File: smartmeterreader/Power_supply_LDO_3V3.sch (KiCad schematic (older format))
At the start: 5 parts

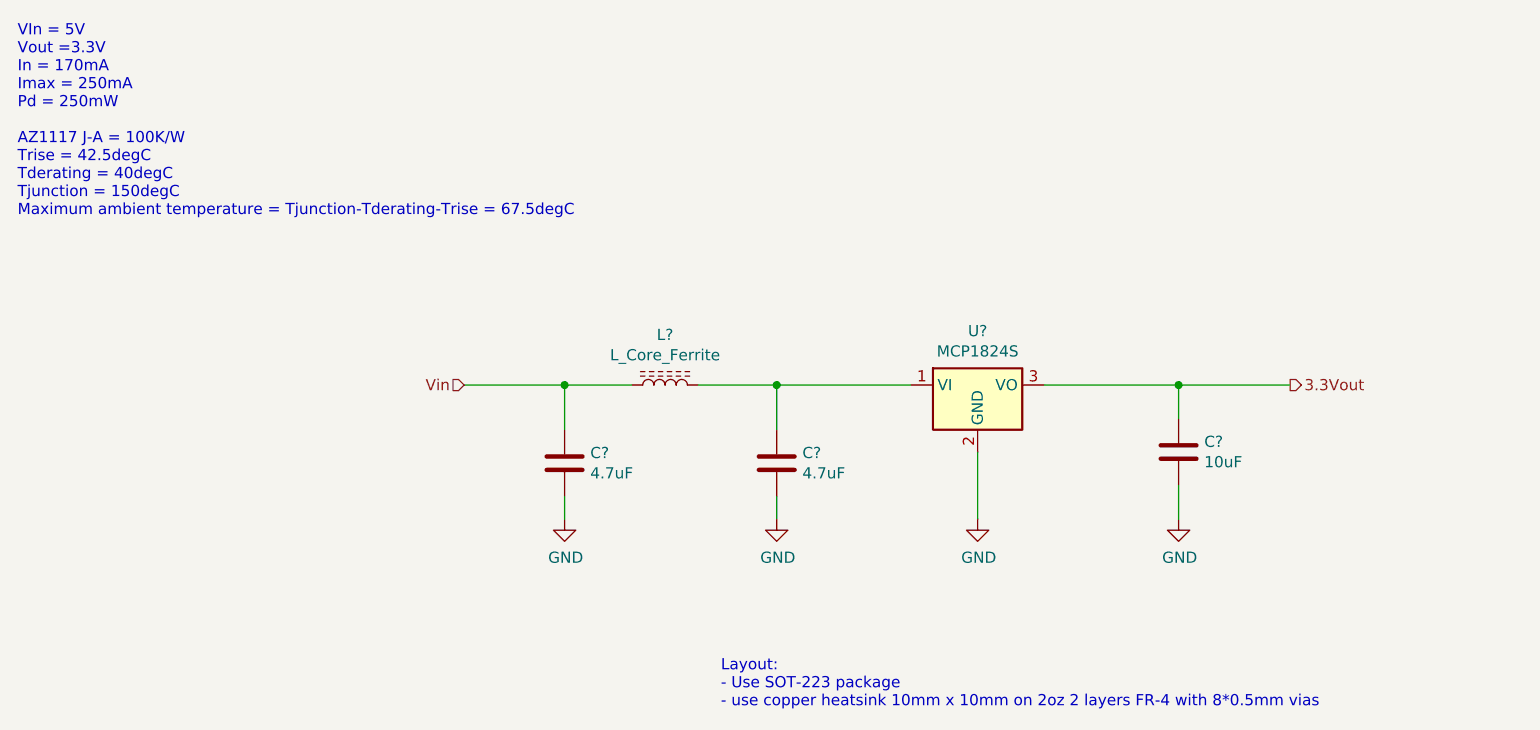
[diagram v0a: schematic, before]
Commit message: Initial version of the smart meter. -Needs compoonent review, - Needs schematics review - No layout
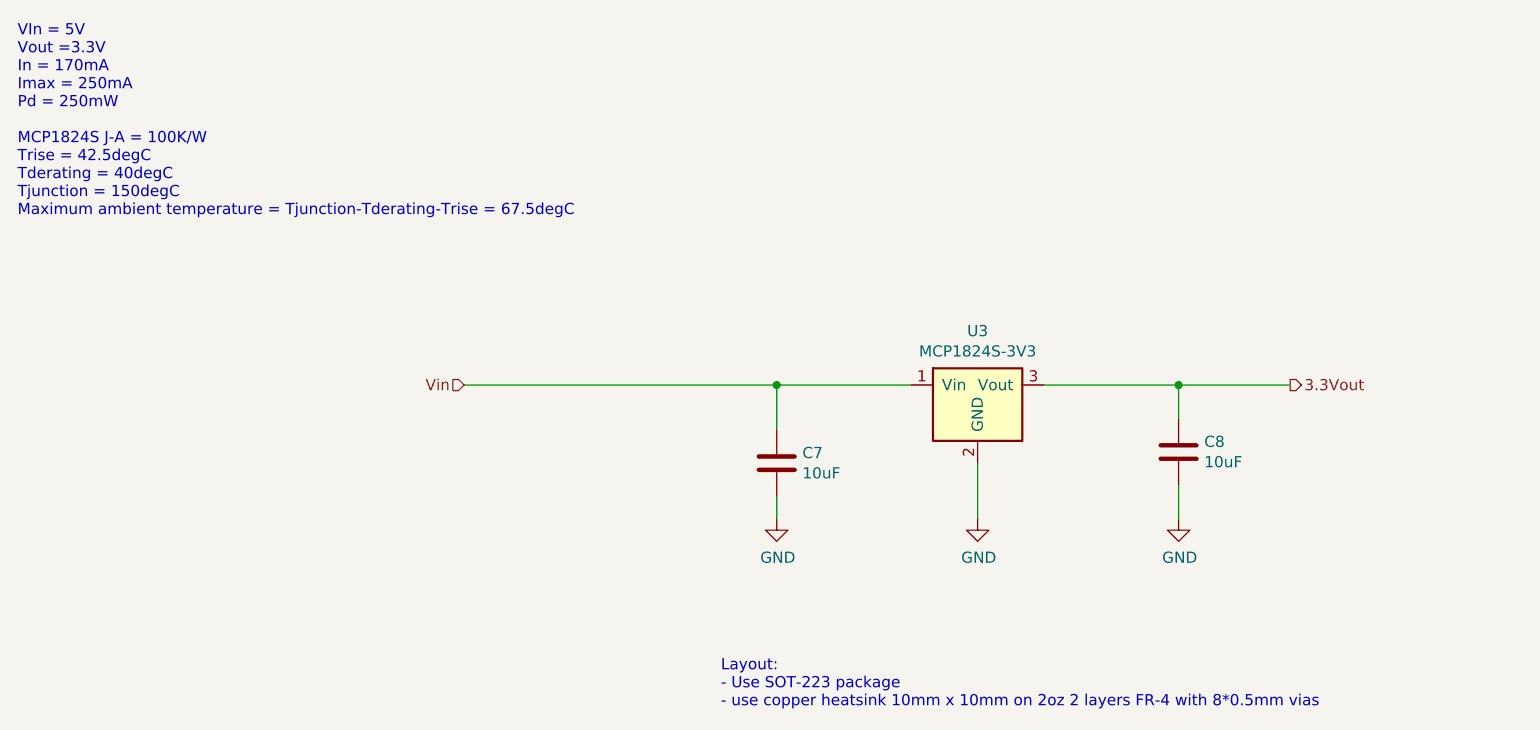
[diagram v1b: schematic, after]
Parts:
- removed C? (x2): 4.7uF, Capacitor_SMD:C_0805_2012Metric, symbol Capacitor_Ceramic_SMD_0603:4.7uF
- removed C?: 10uF, Capacitor_SMD:C_0805_2012Metric, symbol Capacitor_Ceramic_SMD_0603:10uF
- removed L?: L_Core_Ferrite, symbol Device:L_Core_Ferrite
- removed U?: MCP1824S, symbol Regulator_Linear:MCP1825S
- added C7, C8: 10uF, Capacitor_SMD:C_0805_2012Metric, symbol Capacitor_Ceramic_SMD_0603:10uF
- added U3: MCP1824S-3V3, Package_TO_SOT_SMD:SOT-223-3_TabPin2, symbol IC_Power_Regulator:MCP1824S-3V3
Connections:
- net 3.3Vout: now also C8.1, U3.3 (Vout)
- net GND: now also C7.2, C8.2, U3.2 (GND)
- net Vin: now also C7.1, U3.1 (Vin)
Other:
- note added: "VIn = 5V\nVout =3.3V\nIn = 170mA\nImax = 250mA\nPd = 250mW\n\nMCP1824S J-A = 100K/W\nTrise = 42.5degC\nTderating = 40degC\nTjunction = 150degC\nMaximum ambient temperature = Tjunction-Tderating-Trise = 67.5degC"
- note removed: "VIn = 5V\nVout =3.3V\nIn = 170mA\nImax = 250mA\nPd = 250mW\n\nAZ1117 J-A = 100K/W\nTrise = 42.5degC\nTderating = 40degC\nTjunction = 150degC\nMaximum ambient temperature = Tjunction-Tderating-Trise = 67.5degC"
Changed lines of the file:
@@
 $Descr A4 11693 8268
 encoding utf-8
-Sheet 3 3
-Title ""
+Sheet 3 5
+Title "Power supply LDO 300mA 200mV droput"
 Date ""
 Rev ""
-Comp ""
-Comment1 ""
+Comp "ODiaz"
+Comment1 "Orlando Diaz"
 Comment2 ""
 Comment3 ""
@@
 $EndDescr
 Text Notes 1550 2650 0    50   ~ 0
-VIn = 5V\nVout =3.3V\nIn = 170mA\nImax = 250mA\nPd = 250mW\n\nAZ1117 J-A = 100K/W\nTrise = 42.5degC\nTderating = 40degC\nTjunction = 150degC\nMaximum ambient temperature = Tjunction-Tderating-Trise = 67.5degC
+VIn = 5V\nVout =3.3V\nIn = 170mA\nImax = 250mA\nPd = 250mW\n\nMCP1824S J-A = 100K/W\nTrise = 42.5degC\nTderating = 40degC\nTjunction = 150degC\nMaximum ambient temperature = Tjunction-Tderating-Trise = 67.5degC
 Text Notes 4700 4850 0    50   ~ 0
 Layout:\n- Use SOT-223 package\n- use copper heatsink 10mm x 10mm on 2oz 2 layers FR-4 with 8*0.5mm vias
+Wire Wire Line
+	4950 3600 4950 3400
+Wire Wire Line
+	6750 3400 6750 3550
 $Comp
-L Regulator_Linear:MCP1825S U?
-U 1 1 61B7A6BC
+L power:GND #PWR019
+U 1 1 61B7D793
+P 5850 4000
+F 0 "#PWR019" H 5850 3750 50  0001 C CNN
+F 1 "GND" H 5855 3827 50  0000 C CNN
+F 2 "" H 5850 4000 50  0001 C CNN
+F 3 "" H 5850 4000 50  0001 C CNN
+	1    5850 4000
+	1    0    0    -1
+$EndComp
+$Comp
+L power:GND #PWR018
+U 1 1 61B7DB62
+P 4950 4000
+F 0 "#PWR018" H 4950 3750 50  0001 C CNN
+F 1 "GND" H 4955 3827 50  0000 C CNN
+F 2 "" H 4950 4000 50  0001 C CNN
+F 3 "" H 4950 4000 50  0001 C CNN
+	1    4950 4000
+	1    0    0    -1
+$EndComp
+$Comp
+L power:GND #PWR020
+U 1 1 61B7DED9
+P 6750 4000
+F 0 "#PWR020" H 6750 3750 50  0001 C CNN
+F 1 "GND" H 6755 3827 50  0000 C CNN
+F 2 "" H 6750 4000 50  0001 C CNN
+F 3 "" H 6750 4000 50  0001 C CNN
+	1    6750 4000
+	1    0    0    -1
+$EndComp
+Wire Wire Line
+	6750 4000 6750 3850
+Wire Wire Line
+	5850 4000 5850 3750
+Wire Wire Line
+	4950 4000 4950 3900
+Wire Wire Line
+	6150 3400 6750 3400
+Text HLabel 7250 3400 2    50   Output ~ 0
+3.3Vout
+Text HLabel 3550 3400 0    50   Input ~ 0
+Vin
+Wire Wire Line
+	6750 3400 7250 3400
+Connection ~ 6750 3400
+Wire Wire Line
+	4950 3400 5550 3400
+$Comp
+L IC_Power_Regulator:MCP1824S-3V3 U3
+U 1 1 61C6B449
 P 5850 3400
-F 0 "U?" H 5850 3642 50  0000 C CNN
-F 1 "MCP1824S" H 5850 3551 50  0000 C CNN
-F 2 "" H 5750 3550 50  0001 C CNN
-F 3 "http://ww1.microchip.com/downloads/en/devicedoc/22056b.pdf" H 5850 3650 50  0001 C CNN
+F 0 "U3" H 5850 3642 50  0000 C CNN
+F 1 "MCP1824S-3V3" H 5850 3551 50  0000 C CNN
+F 2 "Package_TO_SOT_SMD:SOT-223-3_TabPin2" H 5400 3600 50  0001 C CNN
+F 3 "https://eu.mouser.com/datasheet/2/268/22070a-53890.pdf" H 5850 3400 50  0001 C CNN
+F 4 "MCP1824ST-3302E/DB" H 5750 3700 50  0001 C CNN "MPN"
+F 5 "Microchip" H 5850 3400 50  0001 C CNN "Manufacturer"
+F 6 "300 mA,200mV dropout, 3.3V, SOT-223-3, Low Voltage, Low Quiescent Current LDO Regulator" H 5450 3700 50  0001 C CNN "Description"
+F 7 "NI" H 5850 3400 50  0001 C CNN "Installed"
+F 8 "0" H 5850 3400 50  0001 C CNN "Generic"
+F 9 "No" H 5850 3400 50  0001 C CNN "Reviewed"
 	1    5850 3400
 	1    0    0    -1
 $EndComp
 $Comp
-L Capacitor_Ceramic_SMD_0603:4.7uF C?
-U 1 1 61B7B360
-P 4950 3750
-F 0 "C?" H 5065 3796 50  0000 L CNN
-F 1 "4.7uF" H 5065 3705 50  0000 L CNN
-F 2 "Capacitor_SMD:C_0805_2012Metric" H 4988 3600 50  0001 C CNN
-F 3 "~" H 4950 3750 50  0001 C CNN
-F 4 "GRM219R6YA475MA73D" H 4950 3750 50  0001 C CNN "MPN"
-F 5 "Murata" H 4950 3750 50  0001 C CNN "Manufacturer"
-F 6 "4.7uF 10% 35V X5R 0805" H 4950 3750 50  0001 C CNN "Description"
-F 7 "1" H 4950 3750 50  0001 C CNN "Generic"
-F 8 "NI" H 4950 3750 50  0001 C CNN "Installed"
-	1    4950 3750
-	1    0    0    -1
-$EndComp
-$Comp
-L Capacitor_Ceramic_SMD_0603:10uF C?
-U 1 1 61B7BF43
+L Capacitor_Ceramic_SMD_0603:10uF C8
+U 1 1 61C6E570
 P 6750 3700
-F 0 "C?" H 6865 3746 50  0000 L CNN
+F 0 "C8" H 6865 3746 50  0000 L CNN
 F 1 "10uF" H 6865 3655 50  0000 L CNN
 F 2 "Capacitor_SMD:C_0805_2012Metric" H 6788 3550 50  0001 C CNN
@@
 	1    0    0    -1
 $EndComp
-Wire Wire Line
-	4950 3600 4950 3400
-Wire Wire Line
-	6750 3400 6750 3550
 $Comp
-L power:GND #PWR?
-U 1 1 61B7D793
-P 5850 4000
-F 0 "#PWR?" H 5850 3750 50  0001 C CNN
-F 1 "GND" H 5855 3827 50  0000 C CNN
-F 2 "" H 5850 4000 50  0001 C CNN
-F 3 "" H 5850 4000 50  0001 C CNN
-	1    5850 4000
-	1    0    0    -1
-$EndComp
-$Comp
-L power:GND #PWR?
-U 1 1 61B7DB62
-P 4950 4000
-F 0 "#PWR?" H 4950 3750 50  0001 C CNN
-F 1 "GND" H 4955 3827 50  0000 C CNN
-F 2 "" H 4950 4000 50  0001 C CNN
-F 3 "" H 4950 4000 50  0001 C CNN
-	1    4950 4000
-	1    0    0    -1
-$EndComp
-$Comp
-L power:GND #PWR?
-U 1 1 61B7DED9
-P 6750 4000
-F 0 "#PWR?" H 6750 3750 50  0001 C CNN
-F 1 "GND" H 6755 3827 50  0000 C CNN
-F 2 "" H 6750 4000 50  0001 C CNN
-F 3 "" H 6750 4000 50  0001 C CNN
-	1    6750 4000
+L Capacitor_Ceramic_SMD_0603:10uF C7
+U 1 1 61C6F8D2
+P 4950 3750
+F 0 "C7" H 5065 3796 50  0000 L CNN
+F 1 "10uF" H 5065 3705 50  0000 L CNN
+F 2 "Capacitor_SMD:C_0805_2012Metric" H 4988 3600 50  0001 C CNN
+F 3 "~" H 4950 3750 50  0001 C CNN
+F 4 "GRM21BR6YA106KE43L " H 4950 3750 50  0001 C CNN "MPN"
+F 5 "Murata" H 4950 3750 50  0001 C CNN "Manufacturer"
+F 6 "10uF 10% 35V X5R 0805" H 4950 3750 50  0001 C CNN "Description"
+F 7 "1" H 4950 3750 50  0001 C CNN "Generic"
+F 8 "NI" H 4950 3750 50  0001 C CNN "Installed"
+	1    4950 3750
 	1    0    0    -1
 $EndComp
 Wire Wire Line
-	6750 4000 6750 3850
-Wire Wire Line
-	5850 4000 5850 3700
-Wire Wire Line
-	4950 4000 4950 3900
-Wire Wire Line
-	6150 3400 6750 3400
-$Comp
-L Device:L_Core_Ferrite L?
-U 1 1 61B806F3
-P 4450 3400
-F 0 "L?" V 4675 3400 50  0000 C CNN
-F 1 "L_Core_Ferrite" V 4584 3400 50  0000 C CNN
-F 2 "" H 4450 3400 50  0001 C CNN
-F 3 "~" H 4450 3400 50  0001 C CNN
-	1    4450 3400
-	0    -1   -1   0
-$EndComp
-$Comp
-L Capacitor_Ceramic_SMD_0603:4.7uF C?
-U 1 1 61B823AF
-P 4000 3750
-F 0 "C?" H 4115 3796 50  0000 L CNN
-F 1 "4.7uF" H 4115 3705 50  0000 L CNN
-F 2 "Capacitor_SMD:C_0805_2012Metric" H 4038 3600 50  0001 C CNN
-F 3 "~" H 4000 3750 50  0001 C CNN
-F 4 "GRM219R6YA475MA73D" H 4000 3750 50  0001 C CNN "MPN"
-F 5 "Murata" H 4000 3750 50  0001 C CNN "Manufacturer"
-F 6 "4.7uF 10% 35V X5R 0805" H 4000 3750 50  0001 C CNN "Description"
-F 7 "1" H 4000 3750 50  0001 C CNN "Generic"
-F 8 "NI" H 4000 3750 50  0001 C CNN "Installed"
-	1    4000 3750
-	1    0    0    -1
-$EndComp
-Wire Wire Line
-	4000 3600 4000 3400
-$Comp
-L power:GND #PWR?
-U 1 1 61B83001
-P 4000 4000
-F 0 "#PWR?" H 4000 3750 50  0001 C CNN
-F 1 "GND" H 4005 3827 50  0000 C CNN
-F 2 "" H 4000 4000 50  0001 C CNN
-F 3 "" H 4000 4000 50  0001 C CNN
-	1    4000 4000
-	1    0    0    -1
-$EndComp
-Wire Wire Line
-	4000 4000 4000 3900
-Text HLabel 7250 3400 2    50   Output ~ 0
-3.3Vout
-Text HLabel 3550 3400 0    50   Input ~ 0
-Vin
-Wire Wire Line
-	3550 3400 4000 3400
-Connection ~ 4000 3400
-Wire Wire Line
-	4000 3400 4300 3400
-Wire Wire Line
-	6750 3400 7250 3400
-Connection ~ 6750 3400
-Wire Wire Line
-	4950 3400 5550 3400
+	3550 3400 4950 3400
 Connection ~ 4950 3400
-Wire Wire Line
-	4600 3400 4950 3400
 $EndSCHEMATC
